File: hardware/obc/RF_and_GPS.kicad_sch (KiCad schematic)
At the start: 10 parts, among them J601 Conn_01x08_Socket, J602 SMA RA Connector, J603 SMA RA Connector, J604 SMA RA Connector, U601 RFM98PW, U602 S1216V8, U603 GP2S1+

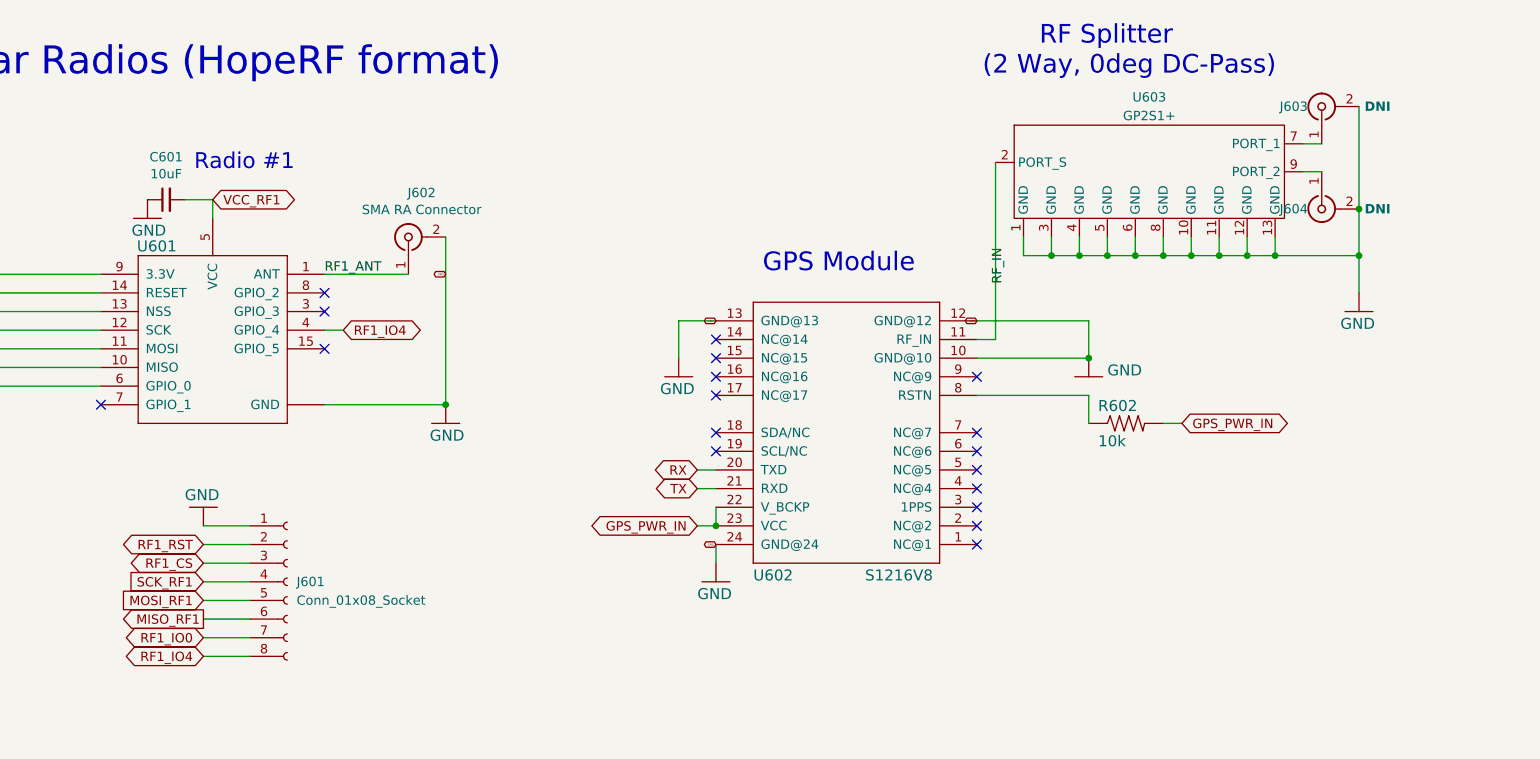
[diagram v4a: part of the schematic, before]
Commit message: obc: BOM editing
Edited the DNI status of several components to be more reflective of our obc setup plans.
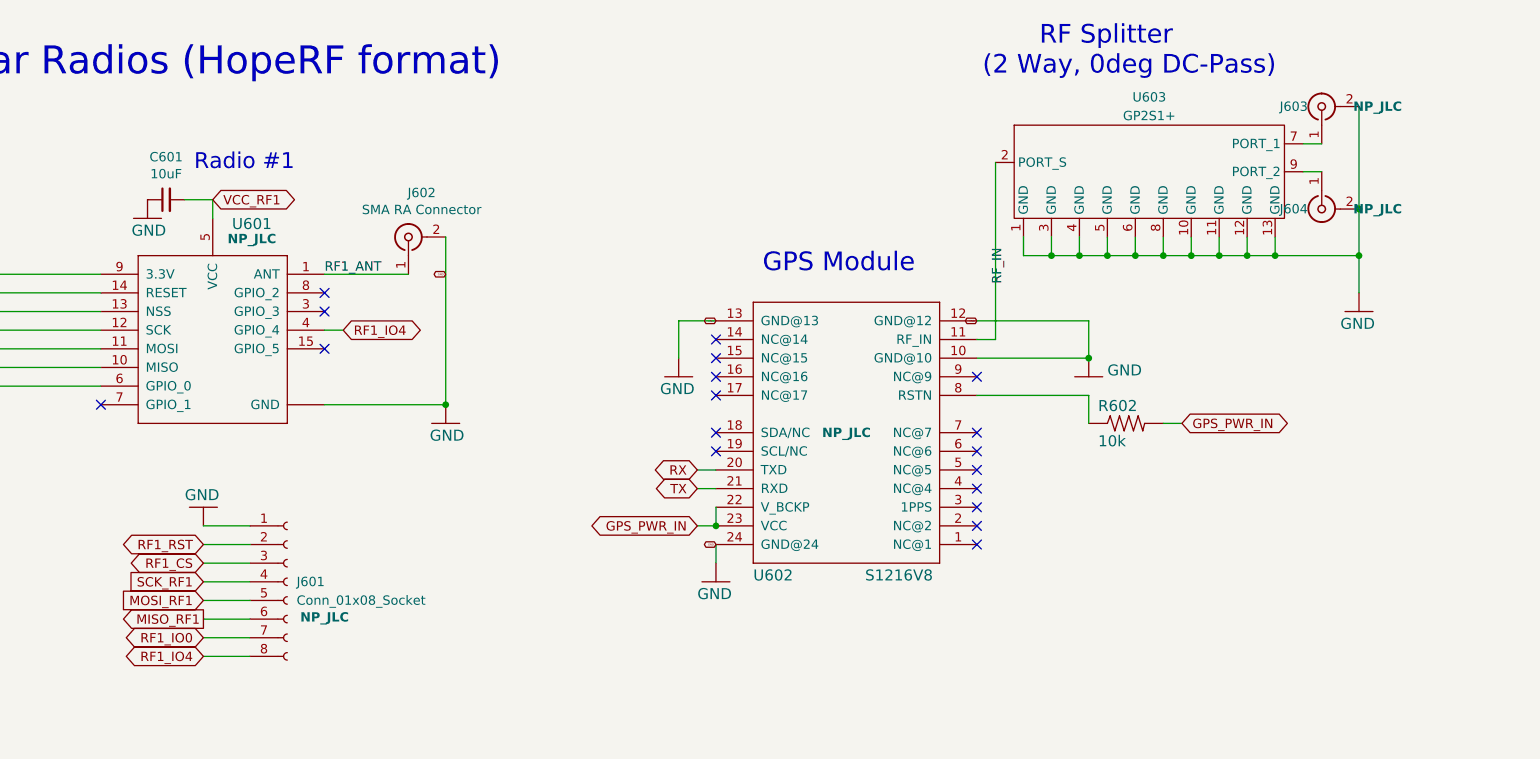
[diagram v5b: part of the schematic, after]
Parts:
- J601: DNI (none) -> NP_JLC; Notes Not placed by JLCPCB -> (none)
- J602: footprint Connector_Coaxial:SMA_Amphenol_901-144_Vertical -> Connector_Coaxial:SMA_Amphenol_132289_EdgeMount; DNI (none) -> NP_JLC; Notes Not placed by JLCPCB -> (none)
- J603, J604: footprint Connector_Coaxial:SMA_Amphenol_901-144_Vertical -> Connector_Coaxial:SMA_Amphenol_132289_EdgeMount; DNI DNI -> NP_JLC; Notes Not placed by JLCPCB -> (none)
- U601: DNI (none) -> NP_JLC; Notes Not placed by JLCPCB (Soldering to back of board) -> (none)
- U602: DNI (none) -> NP_JLC; Manufacturer_Name (none) -> Sky Traq; Manufacturer_Part_Number (none) -> S1216V8
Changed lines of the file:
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@@
 			)
 		)
-		(property "Footprint" "Connector_Coaxial:SMA_Amphenol_901-144_Vertical"
+		(property "Footprint" "Connector_Coaxial:SMA_Amphenol_132289_EdgeMount"
 			(at 237.49 35.56 0)
 			(effects
@@
 			)
 		)
-		(property "DNI" "DNI"
+		(property "DNI" "NP_JLC"
 			(at 245.11 35.56 90)
 			(effects
@@
 			)
 		)
-		(property "Notes" "Not placed by JLCPCB"
+		(property "Notes" ""
 			(at 237.49 35.56 0)
 			(effects
@@
 			)
 		)
-		(property "Footprint" "Connector_Coaxial:SMA_Amphenol_901-144_Vertical"
+		(property "Footprint" "Connector_Coaxial:SMA_Amphenol_132289_EdgeMount"
 			(at 237.49 49.53 0)
 			(effects
@@
 			)
 		)
-		(property "DNI" "DNI"
+		(property "DNI" "NP_JLC"
 			(at 245.11 49.53 90)
 			(effects
@@
 			)
 		)
-		(property "Notes" "Not placed by JLCPCB"
+		(property "Notes" ""
 			(at 237.49 49.53 0)
 			(effects
@@
 			)
 		)
-		(property "Footprint" "Connector_Coaxial:SMA_Amphenol_901-144_Vertical"
+		(property "Footprint" "Connector_Coaxial:SMA_Amphenol_132289_EdgeMount"
 			(at 113.03 53.34 0)
 			(effects
@@
 			)
 		)
-		(property "Notes" "Not placed by JLCPCB"
+		(property "Notes" ""
 			(at 113.03 53.34 0)
 			(effects
@@
 		)
 		(property "Mouser Price/Stock" ""
+			(at 113.03 53.34 0)
+			(effects
+				(font
+					(size 1.27 1.27)
+				)
+				(hide yes)
+			)
+		)
+		(property "DNI" "NP_JLC"
 			(at 113.03 53.34 0)
 			(effects
@@
 		(dnp no)
 		(property "Reference" "U601"
-			(at 78.74 54.61 0)
+			(at 91.694 51.562 0)
 			(effects
 				(font
@@
 			)
 		)
-		(property "Notes" "Not placed by JLCPCB (Soldering to back of board)"
+		(property "Notes" ""
 			(at 83.82 66.04 0)
 			(effects
@@
 				)
 				(hide yes)
+			)
+		)
+		(property "DNI" "NP_JLC"
+			(at 91.694 53.594 0)
+			(effects
+				(font
+					(size 1.27 1.27)
+					(bold yes)
+				)
 			)
 		)
@@
 			)
 		)
-		(property "Description" ""
+		(property "Description" "GPS"
 			(at 172.72 80.01 0)
 			(effects
@@
 			)
 		)
-		(property "DNI" ""
+		(property "DNI" "NP_JLC"
 			(at 172.72 80.01 0)
 			(effects
@@
 		)
 		(property "Mouser Price/Stock" ""
+			(at 172.72 80.01 0)
+			(effects
+				(font
+					(size 1.27 1.27)
+				)
+				(hide yes)
+			)
+		)
+		(property "Manufacturer_Name" "Sky Traq"
+			(at 172.72 80.01 0)
+			(effects
+				(font
+					(size 1.27 1.27)
+				)
+				(hide yes)
+			)
+		)
+		(property "Manufacturer_Part_Number" "S1216V8"
 			(at 172.72 80.01 0)
 			(effects
@@
 		(on_board yes)
 		(dnp no)
-		(fields_autoplaced yes)
 		(property "Reference" "J601"
 			(at 97.79 100.3299 0)
@@
 			)
 		)
-		(property "Notes" "Not placed by JLCPCB"
+		(property "Notes" ""
 			(at 96.52 100.33 0)
 			(effects
@@
 			)
 		)
+		(property "DNI" "NP_JLC"
+			(at 101.6 105.156 0)
+			(effects
+				(font
+					(size 1.27 1.27)
+					(bold yes)
+				)
+			)
+		)

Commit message: obc: preliminary layout complete
Finished preliminary layout of components onto pcb. Entered revised SMA connector into design, however, there is confusion with regards to board cutouts.
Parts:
- J602, J603, J604: footprint Connector_Coaxial:SMA_Amphenol_132289_EdgeMount -> SSE_Footprints:SAMTEC_MMCXV-J-P-HF-ST-EM1; Manufacturer_Name (none) -> Samtec Inc.; Manufacturer_Part_Number (none) -> MMCXV-J-P-HF-ST-EM1-ND
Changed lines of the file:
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@@
 			)
 		)
-		(property "Footprint" "Connector_Coaxial:SMA_Amphenol_132289_EdgeMount"
+		(property "Footprint" "SSE_Footprints:SAMTEC_MMCXV-J-P-HF-ST-EM1"
 			(at 237.49 35.56 0)
 			(effects
@@
 			)
 		)
-		(property "Manufacturer_Name" ""
+		(property "Manufacturer_Name" "Samtec Inc."
 			(at 231.14 35.56 0)
 			(effects
@@
 			)
 		)
-		(property "Manufacturer_Part_Number" ""
+		(property "Manufacturer_Part_Number" "MMCXV-J-P-HF-ST-EM1-ND "
 			(at 231.14 35.56 0)
 			(effects
@@
 			)
 		)
-		(property "Footprint" "Connector_Coaxial:SMA_Amphenol_132289_EdgeMount"
+		(property "Footprint" "SSE_Footprints:SAMTEC_MMCXV-J-P-HF-ST-EM1"
 			(at 237.49 49.53 0)
 			(effects
@@
 			)
 		)
-		(property "Manufacturer_Name" ""
+		(property "Manufacturer_Name" "Samtec Inc."
 			(at 231.14 49.53 0)
 			(effects
@@
 			)
 		)
-		(property "Manufacturer_Part_Number" ""
+		(property "Manufacturer_Part_Number" "MMCXV-J-P-HF-ST-EM1-ND "
 			(at 231.14 49.53 0)
 			(effects
@@
 			)
 		)
-		(property "Footprint" "Connector_Coaxial:SMA_Amphenol_132289_EdgeMount"
+		(property "Footprint" "SSE_Footprints:SAMTEC_MMCXV-J-P-HF-ST-EM1"
 			(at 113.03 53.34 0)
 			(effects
@@
 			)
 		)
-		(property "Manufacturer_Name" ""
+		(property "Manufacturer_Name" "Samtec Inc."
 			(at 112.2934 47.3202 0)
 			(effects
@@
 			)
 		)
-		(property "Manufacturer_Part_Number" ""
+		(property "Manufacturer_Part_Number" "MMCXV-J-P-HF-ST-EM1-ND "
 			(at 112.2934 47.3202 0)
 			(effects

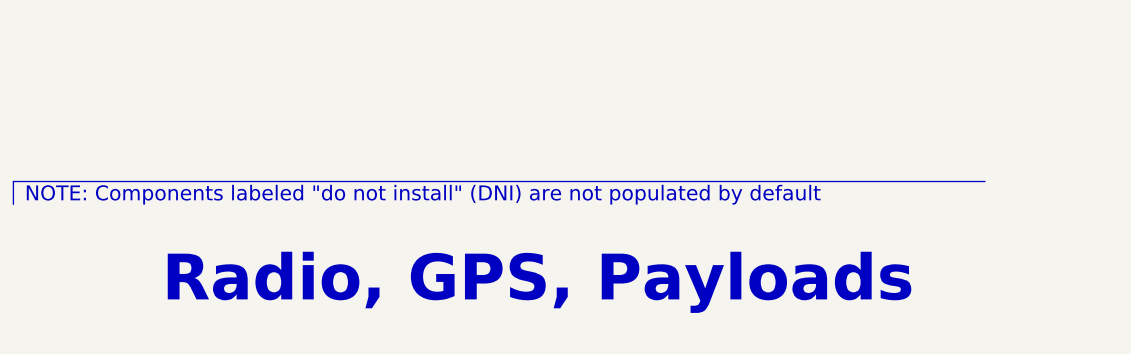
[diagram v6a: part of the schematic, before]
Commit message: obc: power connection cleanup
Decreased track length to vias and centered all vias in pad. Updated schematic title blocks, edited 3D models.
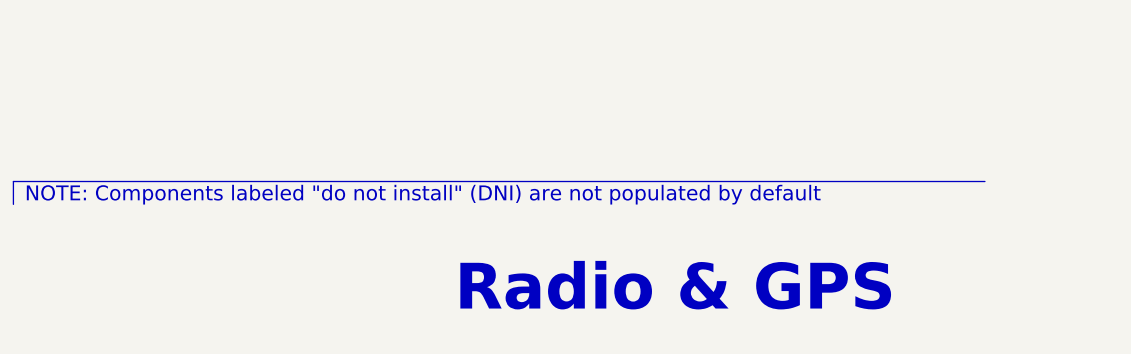
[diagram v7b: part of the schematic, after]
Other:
- note added: "Radio & GPS"
- note removed: "Radio, GPS, Payloads"
- company: Max Holliday -> Ruchir Kavulli, Michael Lyle
- title: PyCubed Mainboard -> Obi Wan Komputer
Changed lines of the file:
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@@
 	(paper "USLetter")
 	(title_block
-		(title "PyCubed Mainboard")
-		(date "2021-06-09")
-		(rev "v05c")
-		(company "Max Holliday")
+		(title "Obi Wan Komputer")
+		(date "2024-06-07")
+		(rev "vA")
+		(company "Ruchir Kavulli, Michael Lyle")
+		(comment 1 "Derived from PyCubed Mainboard v5")
 	)
 	(junction
@@
 		)
 	)
-	(text "Radio, GPS, Payloads"
+	(text "Radio & GPS"
 		(exclude_from_sim no)
-		(at 175.26 182.88 0)
+		(at 207.772 183.896 0)
 		(effects
 			(font

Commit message: obc: test traces for high priority signals
Preliminary trace creation for high priority signals.
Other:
- title: Obi Wan Komputer -> Obi Wan Computer
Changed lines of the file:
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@@
 	(paper "USLetter")
 	(title_block
-		(title "Obi Wan Komputer")
+		(title "Obi Wan Computer")
 		(date "2024-06-07")
 		(rev "vA")
